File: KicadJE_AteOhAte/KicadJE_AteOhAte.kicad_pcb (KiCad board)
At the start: 2 copper layers, 100 x 100 mm, 104 parts, among them J201 In_1, J202 In 2, J203 Out Final, J301 Conn_01x09_Male, J302 Conn_01x09_Male, J303 Out 1, J304 In_1, J305 Out 2, J306 In 2, J307 Out 1 Final, J308 Out 2 Final, P201 Doepfer_Power_10pin, Q201 MMBT2222A, SW201 In or cascade, SW202 Out 1, SW203 In or cascade, SW204 Out 2 FB, SW205 HI/LO, U201 TL072, U202 TL072, U301 TL072, U302 TL072

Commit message: PCB init shape
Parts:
- J201: value In_1 -> In_Accent; footprint AJ-Dropbox-Kicad:PJ301SM -> Connector_Audio:Jack_3.5mm_Ledino_KB3SPRS_Horizontal
- J202: value In 2 -> In Gate; footprint AJ-Dropbox-Kicad:PJ301SM -> Connector_Audio:Jack_3.5mm_Ledino_KB3SPRS_Horizontal
- moved RV202 132.9 mm to (51.9, 92.3)
- moved RV203 124.5 mm to (51.9, 117.5)
- moved RV201 112.3 mm to (51.9, 135.1)
- moved SW202 104.5 mm to (78.8, 119.7)
- moved P201 81.7 mm to (81.6, 93.7)
- moved J201 35.1 mm to (220.2, 55.2)
- moved J202 29.9 mm to (199.3, 55.1)

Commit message: misc
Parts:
- removed the C201 at (196.4, 94.1)
- removed the C204 at (216.4, 79.2)
- removed the J301 at (157.2, 109.1)
- removed the J302 at (161.9, 109.1)
- removed the SW201 at (210.7, 69.0)
- removed SW203: In or cascade, AJ-Dropbox-Kicad:SP1MS1
- removed SW204: Out 2 FB, AJ-Dropbox-Kicad:SP1MS1
- removed SW205: HI/LO, AJ-Dropbox-Kicad:SP1MS1
- added C205: 10n, Capacitor_SMD:C_0805_2012Metric_Pad1.15x1.40mm_HandSolder, F.Cu at (60.1, 33.5)
- added D205: 1N1007, Diode_SMD:D_SOD-123, F.Cu at (54.2, 38.3)
- added Q201: MMBT2222A, Package_TO_SOT_SMD:SOT-23_Handsoldering, F.Cu at (54.5, 29.8)
- added Q202: MMBT2222A, Package_TO_SOT_SMD:SOT-23_Handsoldering, F.Cu at (54.5, 34.3)
- added Q204: MMBT2222A, Package_TO_SOT_SMD:SOT-23_Handsoldering, F.Cu at (61.0, 29.8)
- added R205: 100k, Resistor_SMD:R_0805_2012Metric_Pad1.15x1.40mm_HandSolder, F.Cu at (66.6, 29.0)
- added R206: 100k, Resistor_SMD:R_0805_2012Metric_Pad1.15x1.40mm_HandSolder, F.Cu at (53.7, 41.4)
- added R208: 4k7, Resistor_SMD:R_0805_2012Metric_Pad1.15x1.40mm_HandSolder, F.Cu at (59.4, 38.1)
- added R209: 4k7, Resistor_SMD:R_0805_2012Metric_Pad1.15x1.40mm_HandSolder, F.Cu at (64.9, 33.5)
- added R210: 15k, Resistor_SMD:R_0805_2012Metric_Pad1.15x1.40mm_HandSolder, F.Cu at (71.3, 29.0)
- added R211: 10k, Resistor_SMD:R_0805_2012Metric_Pad1.15x1.40mm_HandSolder, F.Cu at (58.4, 41.4)
- added R212: 4k7, Resistor_SMD:R_0805_2012Metric_Pad1.15x1.40mm_HandSolder, F.Cu at (64.2, 36.5)
- added R213: 4k7, Resistor_SMD:R_0805_2012Metric_Pad1.15x1.40mm_HandSolder, F.Cu at (69.6, 31.9)
- added R214: 10k, Resistor_SMD:R_0805_2012Metric_Pad1.15x1.40mm_HandSolder, F.Cu at (76.1, 29.0)
- added R215: 4k7, Resistor_SMD:R_0805_2012Metric_Pad1.15x1.40mm_HandSolder, F.Cu at (69.6, 34.9)
- added R216: 22k, Resistor_SMD:R_0805_2012Metric_Pad1.15x1.40mm_HandSolder, F.Cu at (64.2, 39.4)
- added R217: 10k, Resistor_SMD:R_0805_2012Metric_Pad1.15x1.40mm_HandSolder, F.Cu at (74.4, 31.9)
- added R218: 47k, Resistor_SMD:R_0805_2012Metric_Pad1.15x1.40mm_HandSolder, F.Cu at (63.2, 42.4)
- added R219: 22k, Resistor_SMD:R_0805_2012Metric_Pad1.15x1.40mm_HandSolder, F.Cu at (68.9, 37.8)
- added R220: 100k, Resistor_SMD:R_0805_2012Metric_Pad1.15x1.40mm_HandSolder, F.Cu at (68.9, 40.8)
- added R221: 100k, Resistor_SMD:R_0805_2012Metric_Pad1.15x1.40mm_HandSolder, F.Cu at (74.4, 34.9)
- added R222: 10k, Resistor_SMD:R_0805_2012Metric_Pad1.15x1.40mm_HandSolder, F.Cu at (79.1, 31.9)
- added R223: 100k, Resistor_SMD:R_0805_2012Metric_Pad1.15x1.40mm_HandSolder, F.Cu at (73.7, 37.8)
- added R224: 100k, Resistor_SMD:R_0805_2012Metric_Pad1.15x1.40mm_HandSolder, F.Cu at (67.9, 43.7)
- moved C201 158.2 mm to (44.0, 41.4)
- moved C203 158.2 mm to (39.2, 41.4)
- moved C204 158.2 mm to (34.5, 42.0)
- moved D201 158.2 mm to (23.5, 42.2)
- moved D202 158.2 mm to (17.4, 42.1)
- moved D203 158.2 mm to (29.2, 42.2)
- moved D204 158.2 mm to (11.1, 42.1)
- moved U201 158.2 mm to (28.7, 36.6)
- moved U202 158.2 mm to (41.9, 36.1)
- moved Q203 99.7 mm to (62.6, 20.4)
- moved R201 62.7 mm to (185.8, 33.2)
- moved R202 62.7 mm to (179.8, 39.1)
- moved C202 58.5 mm to (185.3, 44.6)
- moved R203 58.5 mm to (180.6, 44.6)
- moved R204 58.5 mm to (180.6, 47.6)
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- renumbered C202 to C201, C203 to C202, C205 to C203, C206 to C204, J303 to J301, J304 to J302, J305 to J303, J306 to J304, J307 to J305, J308 to J306, Q201 to Q203, R205 to R207, SW202 to SW201
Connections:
- C201 pad 2: /KicadJE_AteOhAte2/-12v -> -12V
- C202 pad 2: /KicadJE_AteOhAte2/-12v -> -12V
- C203 pad 1: /KicadJE_AteOhAte2/+12v -> +12V
- C204 pad 1: /KicadJE_AteOhAte2/+12v -> +12V
- D201 pad 1: /KicadJE_AteOhAte2/-12v -> -12V
- D203 pad 2: /KicadJE_AteOhAte2/+12v -> +12V
- P201 pad 1: /KicadJE_AteOhAte2/-12v -> -12V
- P201 pad 10: /KicadJE_AteOhAte2/+12v -> +12V
- P201 pad 2: /KicadJE_AteOhAte2/-12v -> -12V
- P201 pad 9: /KicadJE_AteOhAte2/+12v -> +12V
- Q203 pad 1: b-1 -> Net-(Q203-Pad1)
- Q203 pad 2: Net-(Q201-Pad2) -> GND
- Q203 pad 3: c3 -> Net-(Q203-Pad3)
- R304 pad 1: /KicadJE_AteOhAte3/POT2_C -> (no net)
- R314 pad 1: /KicadJE_AteOhAte3/POT4_L -> (no net)
- R316 pad 1: /KicadJE_AteOhAte3/POT3_L -> (no net)
- U201 pad 4: /KicadJE_AteOhAte2/+12v -> +12V
- U201 pad 8: /KicadJE_AteOhAte2/-12v -> -12V
- U202 pad 4: /KicadJE_AteOhAte2/+12v -> +12V
- U202 pad 5: (no net) -> Net-(R218-Pad1)
- U202 pad 6: (no net) -> Net-(R223-Pad2)
- U202 pad 7: (no net) -> Net-(R216-Pad1)
- U202 pad 8: /KicadJE_AteOhAte2/-12v -> -12V

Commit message: Test points for adj
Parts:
- added C205: 39n, Capacitor_SMD:C_0805_2012Metric_Pad1.15x1.40mm_HandSolder, B.Cu at (132.0, 40.0)
- added C206: 1u, Capacitor_SMD:C_0805_2012Metric_Pad1.15x1.40mm_HandSolder, B.Cu at (72.0, 59.0)
- added C207: 22u, Capacitor_SMD:C_0805_2012Metric_Pad1.15x1.40mm_HandSolder, B.Cu at (127.2, 40.0)
- added C208: 18n, Capacitor_SMD:C_0805_2012Metric_Pad1.15x1.40mm_HandSolder, B.Cu at (121.2, 35.2)
- added C209: C11, Capacitor_SMD:C_0805_2012Metric_Pad1.15x1.40mm_HandSolder, B.Cu at (23.2, 19.6)
- added C210: C9, Capacitor_SMD:C_0805_2012Metric_Pad1.15x1.40mm_HandSolder, B.Cu at (6.98, 11.3)
- added C211: C10, Capacitor_SMD:C_0805_2012Metric_Pad1.15x1.40mm_HandSolder, B.Cu at (12.7, 14.6)
- added C212: 1n, Capacitor_SMD:C_0805_2012Metric_Pad1.15x1.40mm_HandSolder, B.Cu at (18.5, 19.2)
- added C213: C12, Capacitor_SMD:C_0805_2012Metric_Pad1.15x1.40mm_HandSolder, B.Cu at (11.7, 11.3)
- added C214: C8, Capacitor_SMD:C_0805_2012Metric_Pad1.15x1.40mm_HandSolder, B.Cu at (6.98, 8.32)
- added C215: C6, Capacitor_SMD:C_0805_2012Metric_Pad1.15x1.40mm_HandSolder, B.Cu at (23.9, 22.5)
- added C216: 47n, Capacitor_SMD:C_0805_2012Metric_Pad1.15x1.40mm_HandSolder, B.Cu at (132.0, 43.0)
- added C218: C7, Capacitor_SMD:C_0805_2012Metric_Pad1.15x1.40mm_HandSolder, B.Cu at (17.5, 14.6)
- added C219: C4, Capacitor_SMD:C_0805_2012Metric_Pad1.15x1.40mm_HandSolder, B.Cu at (19.2, 22.5)
- added D205: 1N4148, Diode_SMD:D_SOD-123, B.Cu at (13.2, 17.8)
- added D206: 1N4148, Diode_SMD:D_SOD-123, B.Cu at (7.48, 17.8)
- added D207: 1N4148, Diode_SMD:D_SOD-123, B.Cu at (7.48, 14.4)
- added D208: 1N4148, Diode_SMD:D_SOD-123, B.Cu at (13.9, 22.3)
- added JP201: Jumper, Connector_PinHeader_2.54mm:PinHeader_1x02_P2.54mm_Vertical, F.Cu at (98.0, 28.0)
- added Q201: MMBT2222A, Package_TO_SOT_SMD:SOT-23_Handsoldering, B.Cu at (74.0, 55.0)
- added Q205: MMBT2907A, Package_TO_SOT_SMD:SOT-23_Handsoldering, B.Cu at (53.0, 21.0)
- added Q207: MMBT2222A, Package_TO_SOT_SMD:SOT-23_Handsoldering, B.Cu at (7.83, 21.7)
- added R201: 1M, Resistor_SMD:R_0805_2012Metric_Pad1.15x1.40mm_HandSolder, B.Cu at (121.2, 32.2)
- added R202: 4k7, Resistor_SMD:R_0805_2012Metric_Pad1.15x1.40mm_HandSolder, B.Cu at (116.6, 28.0)
- added R203: 330K, Resistor_SMD:R_0805_2012Metric_Pad1.15x1.40mm_HandSolder, B.Cu at (127.2, 37.0)
- added R204: 100R, Resistor_SMD:R_0805_2012Metric_Pad1.15x1.40mm_HandSolder, B.Cu at (80.0, 59.0)
- added R205: 22k, Resistor_SMD:R_0805_2012Metric_Pad1.15x1.40mm_HandSolder, B.Cu at (125.9, 34.1)
- added R206: 1M, Resistor_SMD:R_0805_2012Metric_Pad1.15x1.40mm_HandSolder, B.Cu at (76.0, 59.0)
- added R207: 22k, Resistor_SMD:R_0805_2012Metric_Pad1.15x1.40mm_HandSolder, B.Cu at (132.0, 37.0)
- added R208: 300R, Resistor_SMD:R_0805_2012Metric_Pad1.15x1.40mm_HandSolder, B.Cu at (130.7, 34.1)
- added R214: 1k, Resistor_SMD:R_0805_2012Metric_Pad1.15x1.40mm_HandSolder, B.Cu at (11.7, 8.32)
- added R215: 470k, Resistor_SMD:R_0805_2012Metric_Pad1.15x1.40mm_HandSolder, B.Cu at (16.5, 11.7)
- added R216: 820k, Resistor_SMD:R_0805_2012Metric_Pad1.15x1.40mm_HandSolder, B.Cu at (6.98, 5.37)
- added R217: 33k, Resistor_SMD:R_0805_2012Metric_Pad1.15x1.40mm_HandSolder, B.Cu at (27.0, 16.6)
- added R222: 470k, Resistor_SMD:R_0805_2012Metric_Pad1.15x1.40mm_HandSolder, B.Cu at (37.5, 19.6)
- added R223: 33k, Resistor_SMD:R_0805_2012Metric_Pad1.15x1.40mm_HandSolder, B.Cu at (26.0, 10.3)
- added R224: 100k, Resistor_SMD:R_0805_2012Metric_Pad1.15x1.40mm_HandSolder, B.Cu at (31.7, 16.6)
- added R225: 1k, Resistor_SMD:R_0805_2012Metric_Pad1.15x1.40mm_HandSolder, B.Cu at (21.2, 5.77)
- added R230: R17, Resistor_SMD:R_0805_2012Metric_Pad1.15x1.40mm_HandSolder, B.Cu at (38.2, 22.5)
- added R231: R18, Resistor_SMD:R_0805_2012Metric_Pad1.15x1.40mm_HandSolder, B.Cu at (26.0, 13.3)
- added R232: 22k, Resistor_SMD:R_0805_2012Metric_Pad1.15x1.40mm_HandSolder, B.Cu at (32.7, 19.6)
- added R233: 4k7, Resistor_SMD:R_0805_2012Metric_Pad1.15x1.40mm_HandSolder, B.Cu at (21.2, 8.72)
- added R234: 100k, Resistor_SMD:R_0805_2012Metric_Pad1.15x1.40mm_HandSolder, B.Cu at (28.7, 22.5)
- added R238: 4k7, Resistor_SMD:R_0805_2012Metric_Pad1.15x1.40mm_HandSolder, B.Cu at (33.4, 22.5)
- added R239: 4k7, Resistor_SMD:R_0805_2012Metric_Pad1.15x1.40mm_HandSolder, B.Cu at (21.2, 11.7)
- added R242: 4k7, Resistor_SMD:R_0805_2012Metric_Pad1.15x1.40mm_HandSolder, B.Cu at (16.5, 5.77)
- added R243: 3k3, Resistor_SMD:R_0805_2012Metric_Pad1.15x1.40mm_HandSolder, B.Cu at (126.1, 31.1)
- added R244: 33k, Resistor_SMD:R_0805_2012Metric_Pad1.15x1.40mm_HandSolder, B.Cu at (126.1, 28.2)
- added R245: 22k, Resistor_SMD:R_0805_2012Metric_Pad1.15x1.40mm_HandSolder, B.Cu at (16.5, 8.72)
- added R248: 2M2, Resistor_SMD:R_0805_2012Metric_Pad1.15x1.40mm_HandSolder, B.Cu at (28.0, 19.6)
- added R249: 33k, Resistor_SMD:R_0805_2012Metric_Pad1.15x1.40mm_HandSolder, B.Cu at (11.7, 5.37)
- added R250: 22k, Resistor_SMD:R_0805_2012Metric_Pad1.15x1.40mm_HandSolder, B.Cu at (22.2, 16.2)
- added RV204: 1M Decay, Potentiometer_THT:Potentiometer_Piher_T-16H_Single_Horizontal, F.Cu at (53.2, 94.5)
- added RV205: 100k A Level, Potentiometer_THT:Potentiometer_Piher_T-16H_Single_Horizontal, F.Cu at (53.2, 114.9)
- added RV206: 100k A Reverb, Potentiometer_THT:Potentiometer_Piher_T-16H_Single_Horizontal, F.Cu at (53.2, 74.0)
- added U201: TL072, AJ-Dropbox-Kicad:AJ_SO-8_5.3x6.2mm_P1.27mm, B.Cu at (74.0, 75.0)
- C201, C202, C203, C204, D201, D204: moved to B.Cu
- C217: renamed from C205; moved to B.Cu
- D202: renamed from D203; moved to B.Cu
- D203: renamed from D202; moved to B.Cu
- D209: renamed from D205; value 1N1007 -> 1N4148; moved to B.Cu
- J202: footprint Connector_Audio:Jack_3.5mm_Ledino_KB3SPRS_Horizontal -> AJ-Dropbox-Kicad:PJ301SM
- J203: value Out Final -> Out Tom
- Q202: renamed from Q201; moved to B.Cu
- Q203: renamed from Q202; moved to B.Cu
- Q204: renamed from Q203; moved to B.Cu
- Q206: renamed from Q204; moved to B.Cu
- R209: renamed from R201; moved to B.Cu
- R210: renamed from R202; moved to B.Cu
- R211: renamed from R203; moved to B.Cu
- R212: renamed from R207; moved to B.Cu
- R213: renamed from R204; moved to B.Cu
- R218: renamed from R205; moved to B.Cu
- R219: renamed from R206; moved to B.Cu
- R220: renamed from R208; moved to B.Cu
- R221: renamed from R209; moved to B.Cu
- R226: renamed from R210; moved to B.Cu
- R227: renamed from R211; moved to B.Cu
- R228: renamed from R212; moved to B.Cu
- R229: renamed from R215; moved to B.Cu
- R235: renamed from R213; moved to B.Cu
- R236: renamed from R217; moved to B.Cu
- R237: renamed from R214; moved to B.Cu
- R240: renamed from R216; moved to B.Cu
- R241: renamed from R219; moved to B.Cu
- R246: renamed from R222; moved to B.Cu
- R247: renamed from R218; moved to B.Cu
- R251: renamed from R220; moved to B.Cu
- R252: renamed from R221; moved to B.Cu
- R253: renamed from R223; moved to B.Cu
- R254: renamed from R224; moved to B.Cu
- RV201: value 20k_Out1 -> 100K; footprint Potentiometer_THT:Potentiometer_China_RK09_Single_Vertical_AJ -> Potentiometer_THT:Potentiometer_Bourns_3296W_Vertical
- RV202: value 20k_Out2 -> 50K; footprint Potentiometer_THT:Potentiometer_China_RK09_Single_Vertical_AJ -> Potentiometer_THT:Potentiometer_Bourns_3296W_Vertical
- RV203: value 20k_final -> 500R Tune; footprint Potentiometer_THT:Potentiometer_China_RK09_Single_Vertical_AJ -> Potentiometer_THT:Potentiometer_Piher_T-16H_Single_Horizontal
- SW201: value Out 1 -> Con/Tom
- U202: renamed from U201; moved to B.Cu
- U203: renamed from U202; moved to B.Cu
- moved J201 189.2 mm to (55.6, 148.4)
- moved R209 163.2 mm to (57.2, 133.7)
- moved R210 158.3 mm to (52.8, 133.7)
- moved J202 153.0 mm to (73.5, 142.1)
- moved R211 140.8 mm to (71.5, 133.7)
- moved C202 140.0 mm to (52.0, 2.00)
- moved R213 135.7 mm to (75.7, 133.7)
- moved J203 118.3 mm to (83.5, 142.1)
- moved R212 117.0 mm to (84.6, 133.7)
- moved RV201 101.5 mm to (99.1, 45.2)
- moved RV202 71.4 mm to (99.1, 38.8)
- moved RV203 64.2 mm to (53.2, 53.3), turned to 180 degrees
- moved C204 41.9 mm to (47.0, 2.00)
- moved R254 40.3 mm to (75.9, 4.27)
- moved R247 37.6 mm to (71.2, 5.62)
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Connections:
- net Net-(Q201-Pad2) renamed /KicadJE_AteOhAte2/PNP_E
- net Net-(R215-Pad1) renamed /KicadJE_AteOhAte2/PNP_B
- Q204 pad 1: Net-(Q203-Pad1) (its old number) -> Net-(Q204-Pad1)
- R212 pad 2: (no net) -> OutTom
- R237 pad 1: GND -> Net-(Q204-Pad1)
- R237 pad 2: Net-(Q203-Pad1) (its old number) -> GND
- R240 pad 2: Net-(Q203-Pad1) (its old number) -> Net-(Q204-Pad1)
- RV201 pad 1: (no net) -> Net-(R201-Pad2)
- RV201 pad 2: (no net) -> Net-(R202-Pad2)
- RV201 pad 3: (no net) -> Net-(RV201-Pad3)
- RV202 pad 1: (no net) -> /KicadJE_AteOhAte2/WhiteNoise
- RV202 pad 2: (no net) -> Net-(JP201-Pad1)
- RV202 pad 3: (no net) -> /KicadJE_AteOhAte2/PinkNoise
- RV203 pad 1: (no net) -> Net-(D205-Pad1)
- RV203 pad 2: (no net) -> Net-(R214-Pad1)
- RV203 pad 3: (no net) -> GND
- SW201 pad 1: (no net) -> GND
- SW201 pad 2: (no net) -> Net-(R230-Pad2)
- SW201 pad 4: (no net) -> Net-(C210-Pad2)
- SW201 pad 5: (no net) -> Net-(C209-Pad1)
- U202 pad 1: (no net) -> Net-(C209-Pad2)
- U202 pad 2: (no net) -> Net-(C210-Pad1)
- U202 pad 3: (no net) -> Net-(R230-Pad1)
- U202 pad 5: (no net) -> GND
- U202 pad 6: (no net) -> Net-(R217-Pad1)
- U202 pad 7: (no net) -> Net-(R217-Pad2)
- U203 pad 1: (no net) -> Net-(C212-Pad2)
- U203 pad 2: (no net) -> Net-(C212-Pad1)
- U203 pad 3: (no net) -> Net-(R233-Pad2)
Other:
- outline, holes or cut-outs redrawn

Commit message: pcb
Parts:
- added TP201: WhiteNoise, TestPoint:TestPoint_Pad_1.5x1.5mm, F.Cu at (85.0, 62.0)
- added TP202: GND, TestPoint:TestPoint_THTPad_2.0x2.0mm_Drill1.0mm, F.Cu at (61.0, 52.0)
- moved R251 127.8 mm to (79.0, 135.0), turned to 180 degrees
- moved R247 127.4 mm to (75.0, 133.0)
- moved D209 124.5 mm to (79.5, 133.0)
- moved C217 120.7 mm to (75.0, 135.0)
- moved R252 120.4 mm to (71.0, 133.0)
- moved C201 117.5 mm to (-15.0, 103.1)
- moved C202 117.5 mm to (-15.0, 98.5)
- moved C203 117.5 mm to (-19.8, 103.1)
- moved C204 117.5 mm to (-20.0, 98.5)
- moved C209 117.5 mm to (-43.8, 116.1)
- moved C210 117.5 mm to (-60.0, 107.8)
- moved C211 117.5 mm to (-54.3, 111.1)
- moved C212 117.5 mm to (-48.5, 115.7)
- moved C213 117.5 mm to (-55.3, 107.8)
- moved C214 117.5 mm to (-60.0, 104.8)
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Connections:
- Q201 pad 3: Net-(Q201-Pad3) -> (no net)
- RV201 pad 3: Net-(RV201-Pad3) -> (no net)
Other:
- board text added: "Reg noise to 130mV"

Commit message: 12V
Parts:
- moved C204 105.7 mm to (81.0, 129.5), turned to 270 degrees
- moved C203 91.0 mm to (63.2, 65.7), turned to 270 degrees
- moved C202 86.0 mm to (67.2, 123.5), turned to 270 degrees
- moved C201 84.7 mm to (63.2, 70.5), turned to 270 degrees
- moved Q205 77.3 mm to (62.5, 106.2), turned to 270 degrees
- moved R253 69.0 mm to (81.0, 125.8), turned to 90 degrees
- moved R254 66.4 mm to (67.0, 133.0)
- moved R218 60.6 mm to (62.8, 140.5), turned to 180 degrees
- moved Q206 60.5 mm to (62.5, 116.0), turned to 90 degrees
- moved R228 58.5 mm to (62.5, 96.5)
- moved C209 56.5 mm to (11.2, 103.1)
- moved C210 56.5 mm to (-5.02, 94.8)
- moved C211 56.5 mm to (0.73, 98.1)
- moved C212 56.5 mm to (6.48, 102.7)
- moved C213 56.5 mm to (-0.27, 94.8)
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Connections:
- SW201 pad 4: Net-(C210-Pad2) -> (no net)
- SW201 pad 6: (no net) -> Net-(C210-Pad2)
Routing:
- net -12V: track 0.00 -> 154.8 mm
- net +12V: track 0.00 -> 145.6 mm
- net /KicadJE_AteOhAte2/WhiteNoise: track 0.00 -> 42.5 mm, vias 0 -> 3
- net GND: track 0.00 -> 21.4 mm
- net Net-(R201-Pad2): track 0.00 -> 15.9 mm
- net /KicadJE_AteOhAte2/PinkNoise: track 0.00 -> 15.1 mm, vias 0 -> 2
- net Net-(R203-Pad2): track 0.00 -> 13.8 mm, vias 0 -> 2
- net Net-(C206-Pad1): track 0.00 -> 12.2 mm
- net Net-(R247-Pad1): track 0.00 -> 7.52 mm
- net Net-(C208-Pad1): track 0.00 -> 6.95 mm
- net Net-(R202-Pad2): track 0.00 -> 6.85 mm
- net Net-(C207-Pad1): track 0.00 -> 6.73 mm
- net Net-(C206-Pad2): track 0.00 -> 6.47 mm
- net Net-(JP201-Pad1): track 0.00 -> 6.19 mm
- net InGate: track 0.00 -> 4.83 mm
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
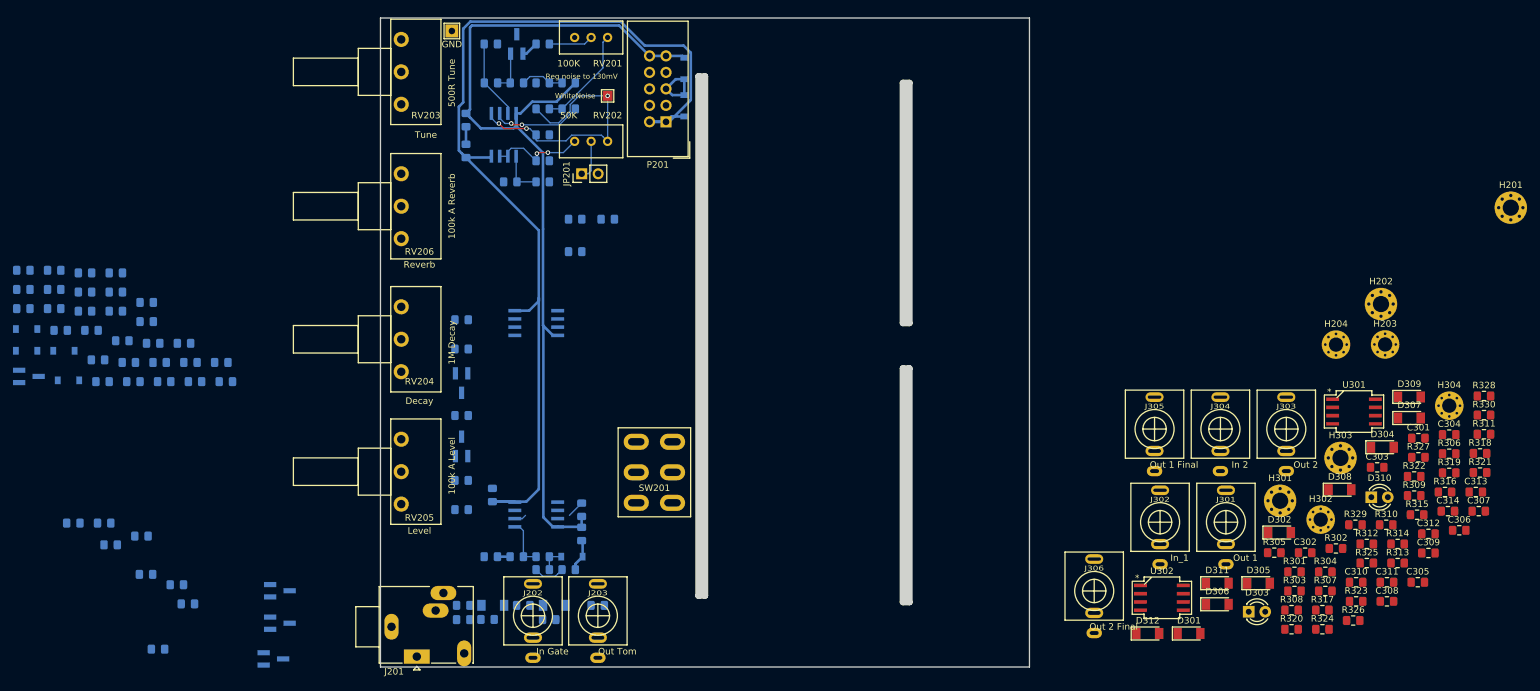
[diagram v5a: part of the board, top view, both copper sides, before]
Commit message: PCB and Testpoint to coupling
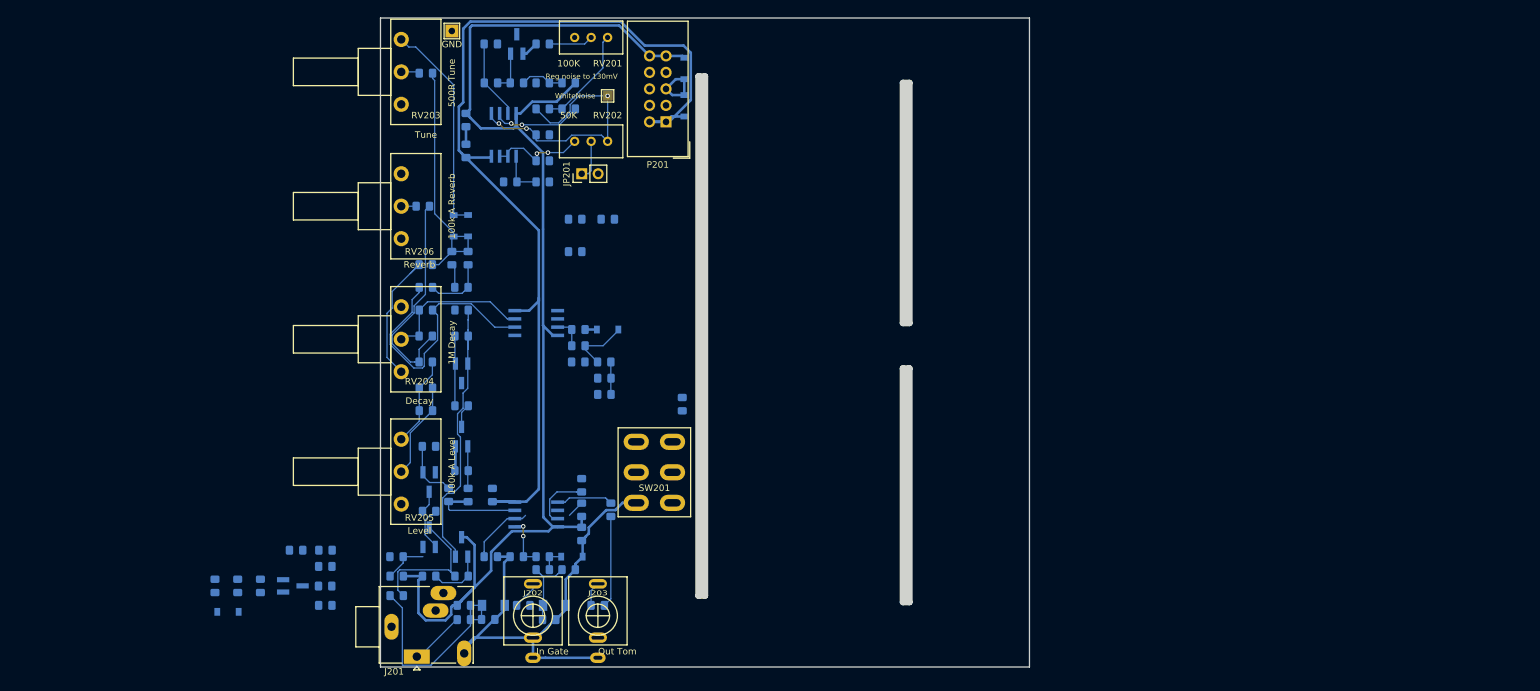
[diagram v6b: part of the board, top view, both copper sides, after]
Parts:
- removed C301, C302, C303, C304: 10n, Capacitor_SMD:C_0805_2012Metric_Pad1.15x1.40mm_HandSolder
- removed C305, C306, C307, C310, C313, C314: 1u, Capacitor_SMD:C_0805_2012Metric_Pad1.15x1.40mm_HandSolder
- removed C308, C309, C311, C312: 100n, Capacitor_SMD:C_0805_2012Metric_Pad1.15x1.40mm_HandSolder
- removed D301, D302, D304, D305, D306, D307, D308, D309: LL4148, Diode_SMD:D_MiniMELF
- removed D303, D310: LED, LED_THT:LED_D3.0mm
- removed D311, D312: D_Zener, Diode_SMD:D_MiniMELF
- removed H201, H202, H301, H303: 2,5mm, MountingHole:MountingHole_2.5mm_Pad_Via
- removed H203, H204, H302, H304: 2,2mm, MountingHole:MountingHole_2.2mm_M2_Pad_Via
- removed J301: Out 1, AJ-Dropbox-Kicad:PJ301SM
- removed J302: In_1, AJ-Dropbox-Kicad:PJ301SM
- removed J303: Out 2, AJ-Dropbox-Kicad:PJ301SM
- removed J304: In 2, AJ-Dropbox-Kicad:PJ301SM
- removed J305: Out 1 Final, AJ-Dropbox-Kicad:PJ301SM
- removed J306: Out 2 Final, AJ-Dropbox-Kicad:PJ301SM
- removed R301, R304, R305, R306, R310, R311, R316, R319, R322, R324: 1k, Resistor_SMD:R_0805_2012Metric_Pad1.15x1.40mm_HandSolder
- removed R302, R303, R307, R308, R312, R314, R317, R318, R327, R329: 10k, Resistor_SMD:R_0805_2012Metric_Pad1.15x1.40mm_HandSolder
- removed R309, R323: 10R, Resistor_SMD:R_0805_2012Metric_Pad1.15x1.40mm_HandSolder
- removed R313, R315: 100k, Resistor_SMD:R_0805_2012Metric_Pad1.15x1.40mm_HandSolder
- removed R320, R321: Open, Resistor_SMD:R_0805_2012Metric_Pad1.15x1.40mm_HandSolder
- removed R325, R326: 0R, Resistor_SMD:R_0805_2012Metric_Pad1.15x1.40mm_HandSolder
- removed R328, R330: OPEN, Resistor_SMD:R_0805_2012Metric_Pad1.15x1.40mm_HandSolder
- removed U301, U302: TL072, AJ-Dropbox-Kicad:AJ_SO-8_5.3x6.2mm_P1.27mm
- moved C214 90.2 mm to (84.5, 103.0)
- moved D207 89.5 mm to (85.0, 98.0), turned to 180 degrees
- moved C209 85.5 mm to (96.5, 109.5), turned to 90 degrees
- moved R225 84.6 mm to (85.5, 125.8), turned to 270 degrees
- moved R233 77.7 mm to (81.0, 122.0), turned to 270 degrees
- moved R239 76.0 mm to (84.5, 105.5)
- moved D206 68.6 mm to (61.3, 82.0), turned to 90 degrees
- moved R216 67.6 mm to (62.5, 91.5), turned to 180 degrees
- moved R231 66.5 mm to (80.5, 98.0)
- moved C210 66.5 mm to (61.0, 87.0), turned to 90 degrees
- moved R214 66.3 mm to (57.0, 58.5)
- moved D205 65.2 mm to (63.5, 82.0), turned to 270 degrees
- moved C211 63.8 mm to (63.5, 87.0), turned to 270 degrees
- moved R242 63.2 mm to (41.5, 140.5)
- moved R238 63.1 mm to (84.5, 108.0)
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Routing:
- net GND: track 21.4 -> 95.0 mm
- net +12V: track 145.6 -> 197.0 mm
- net /KicadJE_AteOhAte2/PNP_E: track 0.00 -> 42.9 mm
- net Net-(R217-Pad1): track 0.00 -> 41.9 mm
- net Net-(C210-Pad2): track 0.00 -> 39.8 mm
- net InAccent: track 0.00 -> 35.5 mm
- net Net-(C213-Pad1): track 0.00 -> 33.7 mm
- net Net-(D205-Pad1): track 0.00 -> 33.3 mm
- net Net-(C212-Pad2): track 0.00 -> 23.7 mm
- net Net-(R217-Pad2): track 0.00 -> 23.3 mm
- net Net-(Q203-Pad3): track 0.00 -> 21.6 mm
- net Net-(R215-Pad1): track 0.00 -> 21.4 mm
- net Net-(R240-Pad1): track 0.00 -> 14.7 mm
- net OutTom: track 0.00 -> 14.1 mm
- net Net-(C212-Pad1): track 0.00 -> 13.9 mm
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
